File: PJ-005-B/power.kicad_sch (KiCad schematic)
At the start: 0 parts

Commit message: Transmitter
-- Preamp 9.5dB gain
-- Power amp 6dB gain
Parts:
- added C1, C3, C5: 10uF,25V, XaltenFootprints:C0603, symbol Device:C
- added C2, C4, C6: 22uF,25V, XaltenFootprints:C0603, symbol Device:C
- added C7, C8: 1uF,25V, XaltenFootprints:C0603, symbol Device:C
- added R1: 680R,1%, XaltenFootprints:R0603, symbol Device:R
- added R2, R4, R7, R8: 100R,1%, XaltenFootprints:R0603, symbol Device:R
- added R3: 390R,1%, XaltenFootprints:R0603, symbol Device:R
- added R5: 430R,1%, XaltenFootprints:R0603, symbol Device:R
- added R6: 140R,1%, XaltenFootprints:R0603, symbol Device:R
- added U1, U2, U3: MIC29302WU-TR, Echosounder Transceiver FP:TO-263-5, symbol Echosounder Transceiver:MIC29302WU-TR
- added U4: MIC5365-2.5YC5-TR, Echosounder Transceiver FP:SC-70, symbol Echosounder Transceiver:MIC5365-2.5YC5-TR
- added U5: LM337IMP/NOPB, Echosounder Transceiver FP:SOT-223, symbol Echosounder Transceiver:LM337IMP_NOPB
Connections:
- new net: R3.2, R4.1, U2.5 (ADJ)
- new net: R1.2, R2.1, U1.5 (ADJ)
- new net: R5.2, R6.1, U3.5 (ADJ)
- new net: R7.2, R8.1, U5.1 (ADJ)
- new net +2V5: C8.1, U4.5 (VOUT)
- new net +5V: C6.1, C7.1, R5.1, U3.4 (OUT), U4.1 (VIN), U4.3 (EN)
- new net -2V5: R7.1, U5.3 (OUT)
- new net -5V: U5.2 (IN), U5.4 (TAB)
- new net 12V: C1.1, U1.1 (EN), U1.2 (IN)
- new net 6V: C4.1, C5.1, R3.1, U2.4 (OUT), U3.1 (EN), U3.2 (IN)
- new net 9V: C2.1, C3.1, R1.1, U1.4 (OUT), U2.1 (EN), U2.2 (IN)
- new net GND: C1.2, C2.2, C3.2, C4.2, C5.2, C6.2, C7.2, C8.2, R2.2, R4.2, R6.2, U1.3 (GND), U1.6 (TAB), U2.3 (GND), U2.6 (TAB), U3.3 (GND), U3.6 (TAB), U4.2 (GND)
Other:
- note added: "LDO, -5V to -2.5V"
- note added: "LDO, 12V to 9V"
- note added: "LDO, 5V to 2.5V"
- note added: "LDO, 6V to 5V"
- note added: "LDO, 9V to 6V"

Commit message: -- Transmitter with pre-amp LM7171 and power amp LT1210 -- Receiver with charge amp-->inverting amp-->4th order filter-->Inverting amp-->buffer -- Power with LDO 12V to 9V, 9V to 6V, 6V to 5V, 5V to 2.5V and -5V to -2.5V
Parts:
- U1, U2, U3: XaltelPartNumber REG-ADJ -> (none); XaltenPartNumber (none) -> REG-ADJ
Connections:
- net GND: now also R8.2
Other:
- company: (none) -> Xalten Systems Pvt. Ltd.
- title: (none) -> Echosounder Transceiver
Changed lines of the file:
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@@
 	(generator_version "9.0")
 	(paper "A3")
+	(title_block
+		(title "Echosounder Transceiver")
+		(date "06-04-2026")
+		(rev "0.1")
+		(company "Xalten Systems Pvt. Ltd.")
+		(comment 1 "Designed by: Varun G")
+	)
 	(text "LDO, -5V to -2.5V"
 		(exclude_from_sim no)
@@
 	(wire
 		(pts
+			(xy 350.52 134.62) (xy 350.52 137.16)
+		)
+		(stroke
+			(width 0)
+			(type default)
+		)
+	)
+	(wire
+		(pts
 			(xy 140.97 46.99) (xy 123.19 46.99)
 		)
@@
 			)
 		)
-		(property "XaltelPartNumber" "REG-ADJ"
+		(property "Supplier" "Element14"
 			(at 95.25 46.99 0)
 			(effects
@@
 			)
 		)
-		(property "Supplier" "Element14"
+		(property "SupplierPartNumber" "2510027"
 			(at 95.25 46.99 0)
 			(effects
@@
 			)
 		)
-		(property "SupplierPartNumber" "2510027"
+		(property "SupplierURL" "https://in.element14.com/microchip/mic29302wu-tr/ldo-reg-26vin-3a-adj-5to263/dp/2510027"
 			(at 95.25 46.99 0)
 			(effects
@@
 			)
 		)
-		(property "SupplierURL" "https://in.element14.com/microchip/mic29302wu-tr/ldo-reg-26vin-3a-adj-5to263/dp/2510027"
+		(property "UnitPriceINR" "264.84"
 			(at 95.25 46.99 0)
 			(effects
@@
 			)
 		)
-		(property "UnitPriceINR" "264.84"
+		(property "OperatingTemperatureRange" "-40C to 125C"
 			(at 95.25 46.99 0)
 			(effects
@@
 			)
 		)
-		(property "OperatingTemperatureRange" "-40C to 125C"
+		(property "XaltenPartNumber" "REG-ADJ"
 			(at 95.25 46.99 0)
 			(effects
@@
 			)
 		)
-		(property "XaltelPartNumber" "REG-ADJ"
+		(property "Supplier" "Element14"
 			(at 95.25 110.49 0)
 			(effects
@@
 			)
 		)
-		(property "Supplier" "Element14"
+		(property "SupplierPartNumber" "2510027"
 			(at 95.25 110.49 0)
 			(effects
@@
 			)
 		)
-		(property "SupplierPartNumber" "2510027"
+		(property "SupplierURL" "https://in.element14.com/microchip/mic29302wu-tr/ldo-reg-26vin-3a-adj-5to263/dp/2510027"
 			(at 95.25 110.49 0)
 			(effects
@@
 			)
 		)
-		(property "SupplierURL" "https://in.element14.com/microchip/mic29302wu-tr/ldo-reg-26vin-3a-adj-5to263/dp/2510027"
+		(property "UnitPriceINR" "264.84"
 			(at 95.25 110.49 0)
 			(effects
@@
 			)
 		)
-		(property "UnitPriceINR" "264.84"
+		(property "OperatingTemperatureRange" "-40C to 125C"
 			(at 95.25 110.49 0)
 			(effects
@@
 			)
 		)
-		(property "OperatingTemperatureRange" "-40C to 125C"
+		(property "XaltenPartNumber" "REG-ADJ"
 			(at 95.25 110.49 0)
 			(effects
@@
 	)
 	(symbol
+		(lib_id "power:GND")
+		(at 350.52 137.16 0)
+		(unit 1)
+		(exclude_from_sim no)
+		(in_bom yes)
+		(on_board yes)
+		(dnp no)
+		(fields_autoplaced yes)
+		(property "Reference" "#PWR058"
+			(at 350.52 143.51 0)
+			(effects
+				(font
+					(size 1.27 1.27)
+				)
+				(hide yes)
+			)
+		)
+		(property "Value" "GND"
+			(at 350.52 142.24 0)
+			(effects
+				(font
+					(size 1.27 1.27)
+				)
+			)
+		)
+		(property "Footprint" ""
+			(at 350.52 137.16 0)
+			(effects
+				(font
+					(size 1.27 1.27)
+				)
+				(hide yes)
+			)
+		)
+		(property "Datasheet" ""
+			(at 350.52 137.16 0)
+			(effects
+				(font
+					(size 1.27 1.27)
+				)
+				(hide yes)
+			)
+		)
+		(property "Description" "Power symbol creates a global label with name \"GND\" , ground"
+			(at 350.52 137.16 0)
+			(effects
+				(font
+					(size 1.27 1.27)
+				)
+				(hide yes)
+			)
+		)
+		(pin "1"
+		)
+		(instances
+			(project "PJ-005-B"
+				(path "/f8bcf36d-3331-4358-bdb9-a545dbff75f1/ec191d7b-699b-4783-a9b8-9c242f8d077f"
+					(reference "#PWR058")
+					(unit 1)
+				)
+			)
+		)
+	)
+	(symbol
 		(lib_id "power:-2V5")
 		(at 356.87 105.41 0)
@@
 			)
 		)
-		(property "XaltelPartNumber" "REG-ADJ"
+		(property "Supplier" "Element14"
 			(at 95.25 177.8 0)
 			(effects
@@
 			)
 		)
-		(property "Supplier" "Element14"
+		(property "SupplierPartNumber" "2510027"
 			(at 95.25 177.8 0)
 			(effects
@@
 			)
 		)
-		(property "SupplierPartNumber" "2510027"
+		(property "SupplierURL" "https://in.element14.com/microchip/mic29302wu-tr/ldo-reg-26vin-3a-adj-5to263/dp/2510027"
 			(at 95.25 177.8 0)
 			(effects
@@
 			)
 		)
-		(property "SupplierURL" "https://in.element14.com/microchip/mic29302wu-tr/ldo-reg-26vin-3a-adj-5to263/dp/2510027"
+		(property "UnitPriceINR" "264.84"
 			(at 95.25 177.8 0)
 			(effects
@@
 			)
 		)
-		(property "UnitPriceINR" "264.84"
+		(property "OperatingTemperatureRange" "-40C to 125C"
 			(at 95.25 177.8 0)
 			(effects
@@
 			)
 		)
-		(property "OperatingTemperatureRange" "-40C to 125C"
+		(property "XaltenPartNumber" "REG-ADJ"
 			(at 95.25 177.8 0)
 			(effects

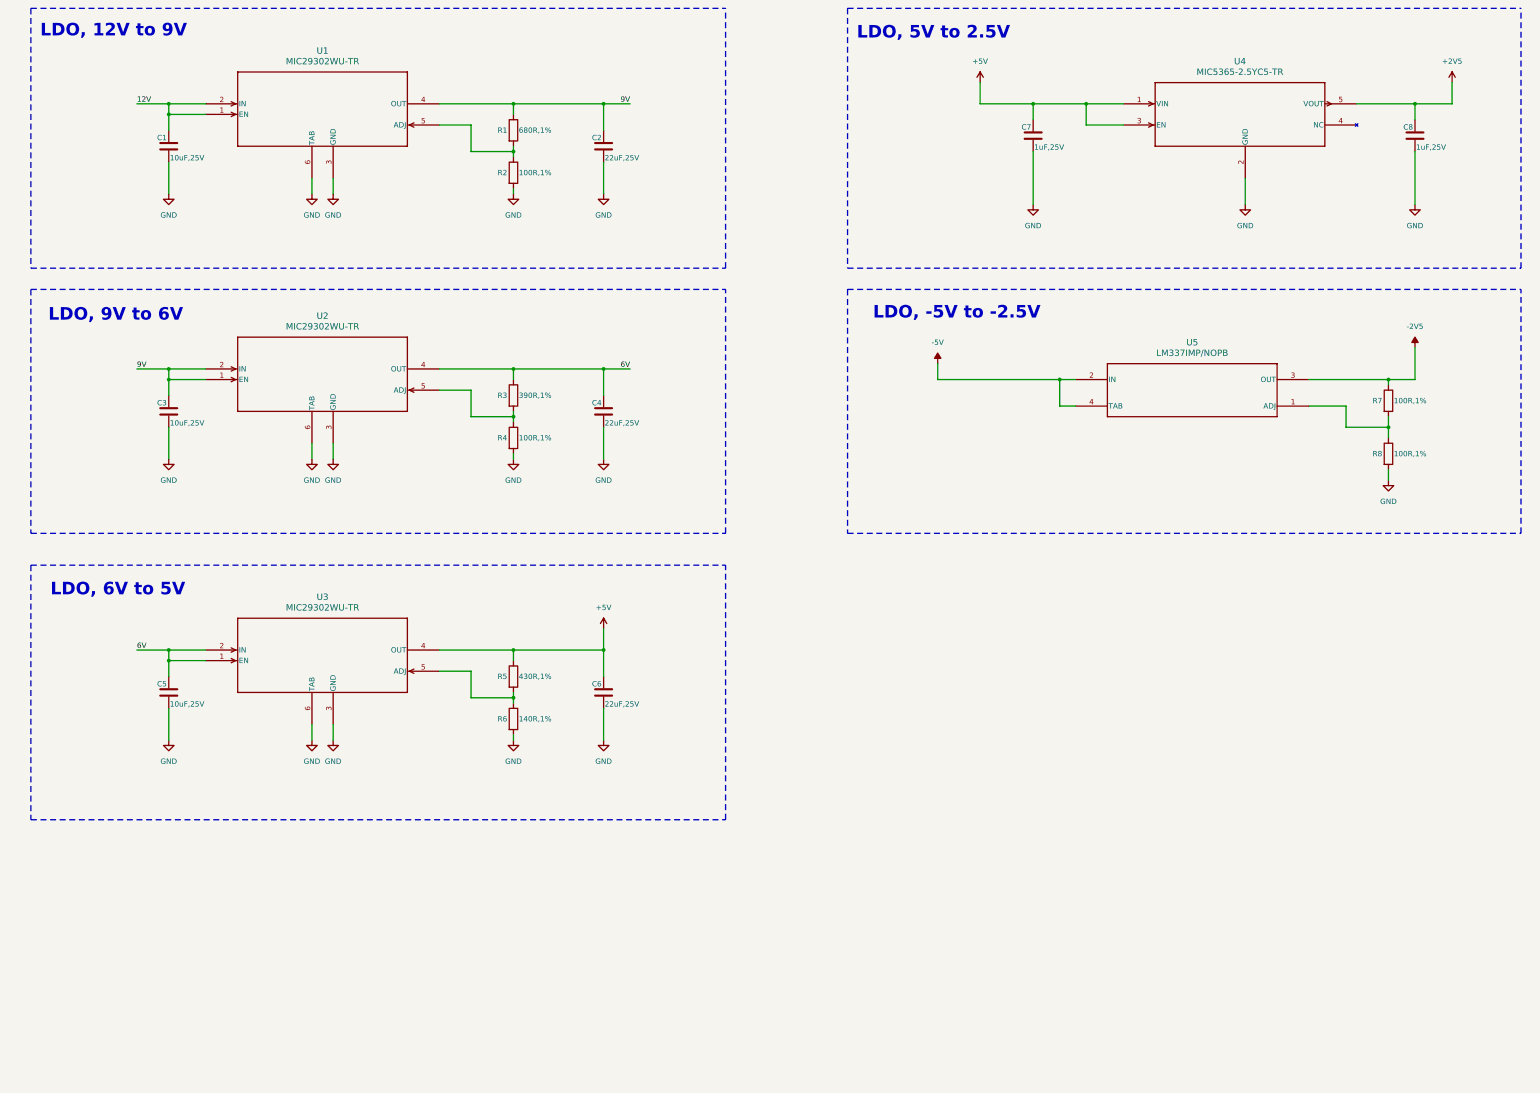
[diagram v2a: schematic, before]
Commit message: -- Receive stage with charge amp-->inverting amp-->BPF-->inverting amp-->buffer-->PGA-->buffer -- Transmit stage with push pull mosfet -- TTL to RS485 converter -- LDOs 12V to 9V, 9V to 6V, 6V to 5V, 5V to 2.5V and -5V to -2.5V
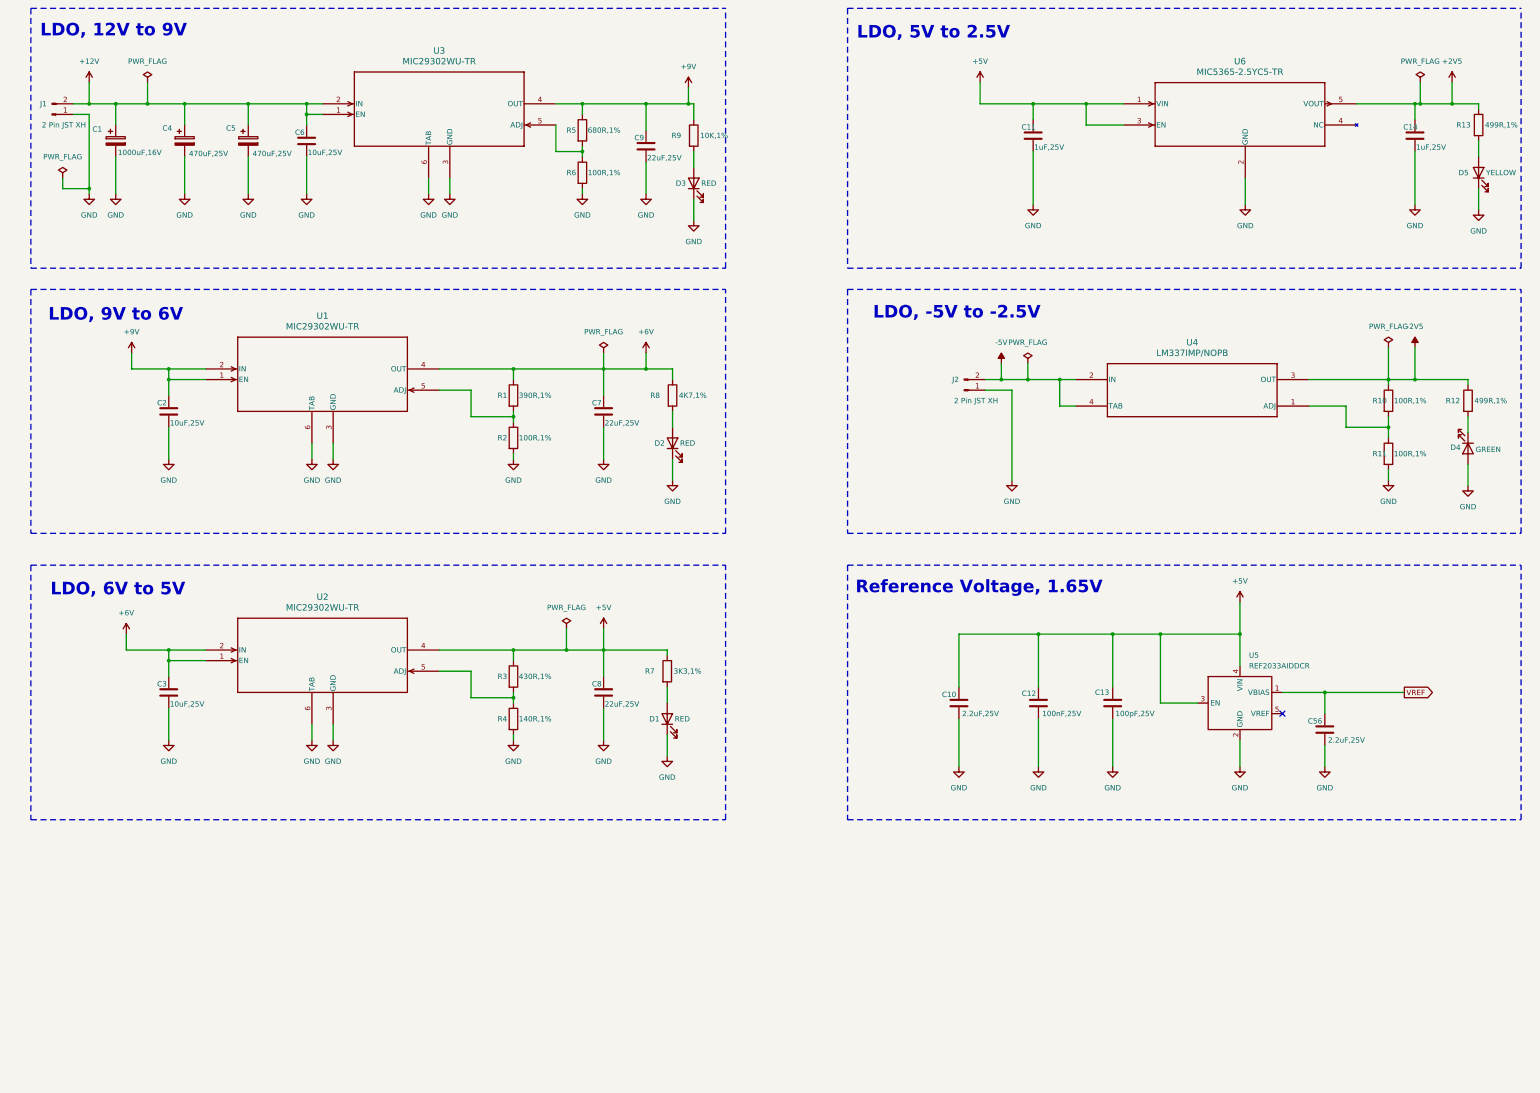
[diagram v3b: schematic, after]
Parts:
- added C1: 1000uF,16V, Capacitor_THT:CP_Radial_D8.0mm_P3.50mm, symbol Device:C_Polarized
- added C10, C56: 2.2uF,25V, XaltenFootprints:C0603, symbol Device:C
- added C12: 100nF,25V, XaltenFootprints:C0603, symbol Device:C
- added C13: 100pF,25V, XaltenFootprints:C0603, symbol Device:C
- added C4, C5: 470uF,25V, Capacitor_THT:CP_Radial_D8.0mm_P3.50mm, symbol Device:C_Polarized
- added D1, D2, D3: RED, LED_SMD:LED_0603_1608Metric, symbol Device:LED
- added D4: GREEN, LED_SMD:LED_0603_1608Metric, symbol Device:LED
- added D5: YELLOW, LED_SMD:LED_0603_1608Metric, symbol Device:LED
- added J1, J2: 2 Pin JST XH, Connector_JST:JST_XH_B2B-XH-A_1x02_P2.50mm_Vertical, symbol Connector:Conn_01x02_Pin
- added R12, R13: 499R,1%, XaltenFootprints:R0603, symbol Device:R
- added R7: 3K3,1%, XaltenFootprints:R0603, symbol Device:R
- added R8: 4K7,1%, XaltenFootprints:R0603, symbol Device:R
- added R9: 10K,1%, XaltenFootprints:R0603, symbol Device:R
- added U5: REF2033AIDDCR, XaltenFootprints:SOT-23-5, symbol Echosounder Transceiver:REF2033AIDDCR
- renumbered C7 to C11, C8 to C14, C3 to C2, C5 to C3, C1 to C6, C4 to C7, C6 to C8, C2 to C9, R3 to R1, R7 to R10, R8 to R11, R4 to R2, R5 to R3, R6 to R4, R1 to R5, R2 to R6, U2 to U1, U3 to U2, U1 to U3, U5 to U4, U4 to U6
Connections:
- net +2V5: now also R13.1
- net +5V: now also C10.1, C12.2, C13.2, R7.1, U5.3 (EN), U5.4 (VIN)
- net -2V5: now also R12.1
- net -5V: now also J2.2 (Pin_2)
- net GND: now also C1.2, C10.2, C12.1, C13.1, C4.2, C5.2, C56.2, D1.1 (K), D2.1 (K), D3.1 (K), D4.2 (A), D5.1 (K), J1.1 (Pin_1), J2.1 (Pin_1), U5.2 (GND)
- net 12V renamed +12V
- net +12V: now also C1.1, C4.1, C5.1, J1.2 (Pin_2)
- net 6V renamed +6V
- net +6V: now also R8.1
- net 9V renamed +9V
- net +9V: now also R9.1
- new net: D2.2 (A), R8.2
- new net: D1.2 (A), R7.2
- new net: D5.2 (A), R13.2
- new net: D3.2 (A), R9.2
- new net: D4.1 (K), R12.2
- new net VREF: C56.1, U5.1 (VBIAS)
- no-connect marks 0 -> 1
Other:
- note added: "Reference Voltage, 1.65V"
- moved on the sheet: C6, C9, R5, R6, U3
